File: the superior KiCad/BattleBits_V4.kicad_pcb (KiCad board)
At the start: 2 copper layers, 140 x 140 mm, 113 parts, among them IC1 4001N, IC10 REG1117, IC11 LM2901D, IC12 LM2901D, IC2 ULN2004AD, IC3 4001N, IC4 ULN2004AD, IC5 ULN2004AD, IC6 ULN2004AD, IC7 ULN2004AD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

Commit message: -
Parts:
- moved R15 5.09 mm to (130.7, 87.4)
- moved R16 0.50 mm to (167.6, 87.4)
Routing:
- net /GND: track 79.1 -> 95.9 mm, vias 4 -> 5
- net Net-(R15-Pad1): track 0.69 -> 10.9 mm
- net /VDD: track 726.3 -> 725.5 mm

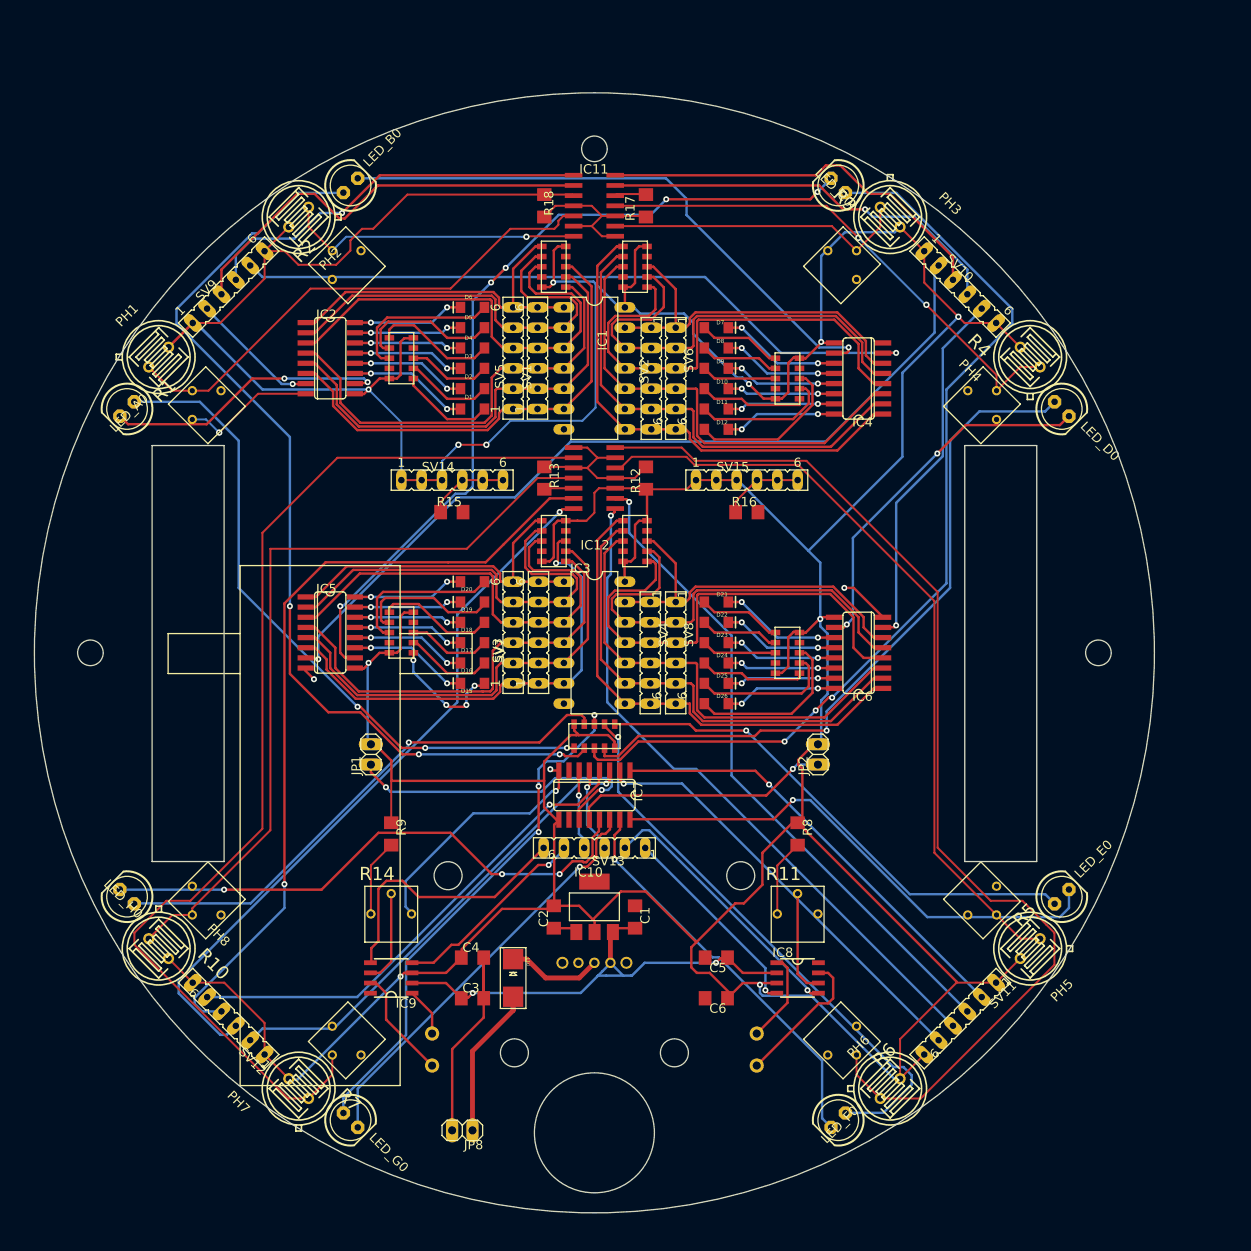
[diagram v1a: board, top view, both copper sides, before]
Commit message: silkscreen added
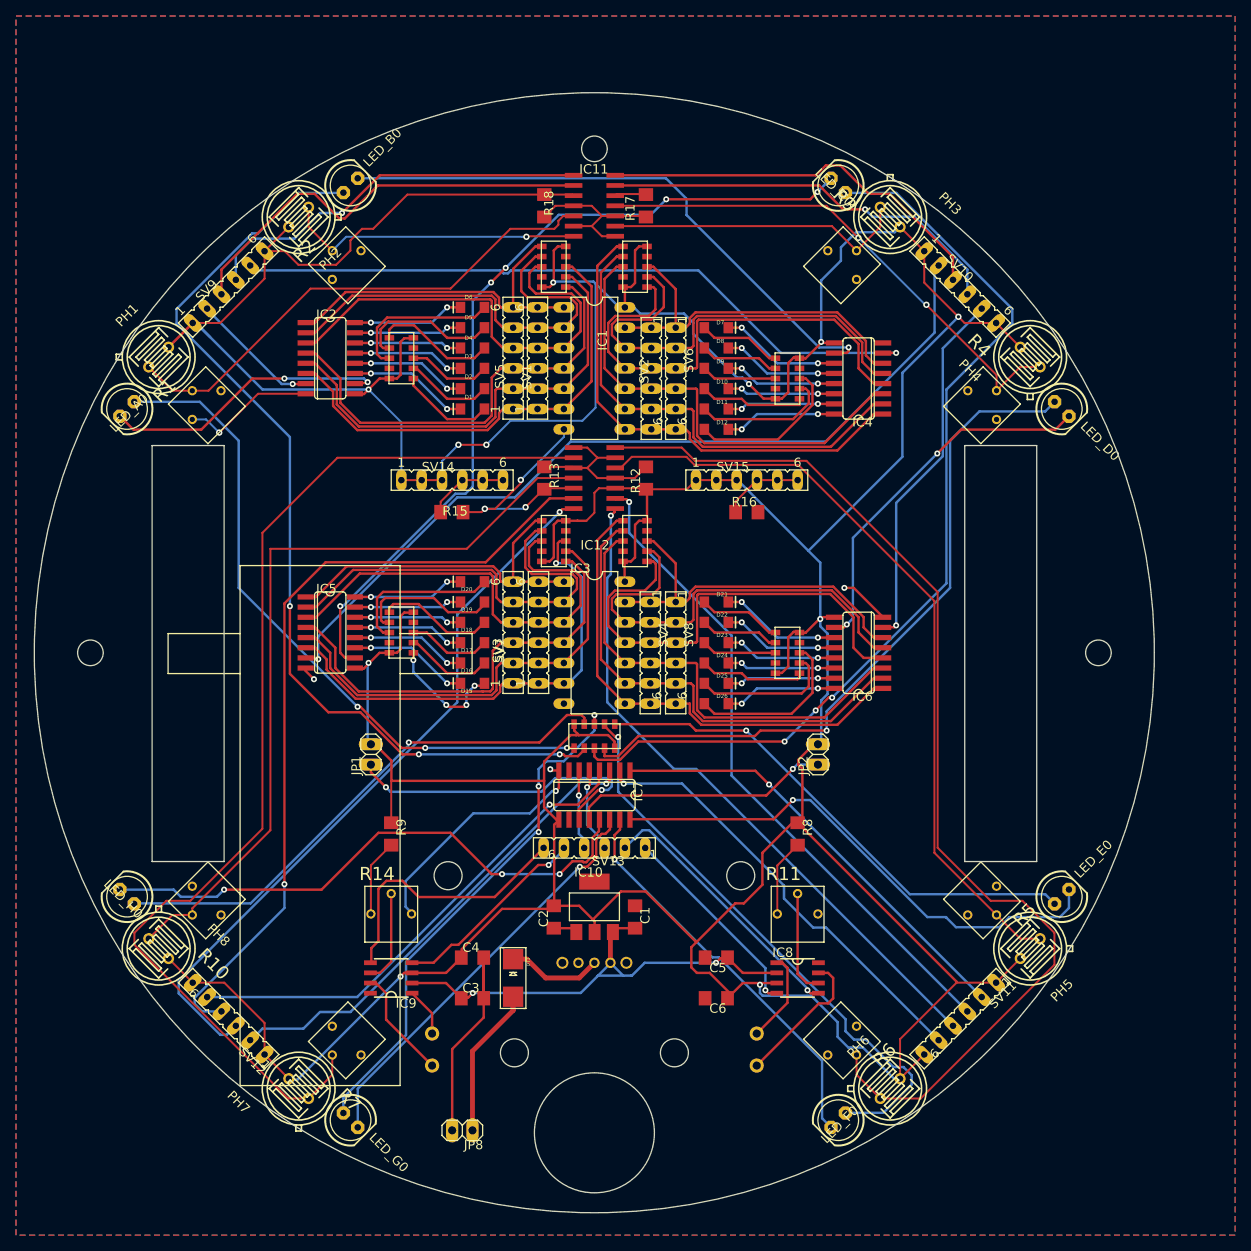
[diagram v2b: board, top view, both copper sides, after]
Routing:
- net /GND: track 95.9 -> 122.1 mm, vias 5 -> 8
- net /VDD: track 725.5 -> 722.4 mm
- net Net-(R16-Pad1): track 11.3 -> 10.2 mm
- net Net-(IC7-Pad16): track 64.8 -> 65.8 mm
- net /LED_CH_F_IN: track 54.5 -> 55.4 mm
- net Net-(LED_F0-PadA): track 71.7 -> 72.6 mm
- net Net-(IC7-Pad13): track 70.1 -> 70.8 mm
- net Net-(R15-Pad1): track 10.9 -> 10.2 mm
- net /LED_CH_A_OUT: track 35.7 -> 36.2 mm
- added copper zone on B.Cu, net /GND
- added copper zone on F.Cu, net /GND
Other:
- board text added: "+"
- board text added: "+V_BAT"
- board text added: "-"
- board text added: "-V_BAT"
- board text added: "0"
- board text added: "1"
- board text added: "10"
- board text added: "11"
- board text added: "12"
- board text added: "13"
- board text added: "14"
- board text added: "2"
- board text added: "3"
- board text added: "4"
- board text added: "5"
- board text added: "6"
- board text added: "7"
- board text added: "8"
- board text added: "9"
- board text added: "Battle Bits PCB V4.0"
- board text added: "Comparator"
- board text added: "Designed by Jelle Reith September 2022"
- board text added: "GND"
- board text added: "GND / Logic 0"
- board text added: "H-Bridge motor driver"
- board text added: "L MOTOR FWD"
- board text added: "L MOTOR REV"
- board text added: "Logic Gate"
- board text added: "MAX 500 mA"
- board text added: "Output A"
- board text added: "Output B"
- board text added: "R MOTOR FWD"
- board text added: "R MOTOR REV"
- board text added: "Resistor Array"
- board text added: "Transistor Array"
- board text added: "VDD"
- board text added: "VDD / Logic 1"

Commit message: gerber
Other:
- board text added: "BattleBits PCB V4.0"
- board text added: "BattleBits PCB V4.0 battlebits.org"
- board text added: "Black wire"
- board text added: "Red wire"
- board text added: "battlebits.org"
- board text added: "battlebits.org jellereith.nl iboibelings.nl"
- board text removed: "Battle Bits PCB V4.0"
